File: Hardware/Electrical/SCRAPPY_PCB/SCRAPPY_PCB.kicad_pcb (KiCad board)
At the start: 2 copper layers, 87.6 x 96.5 mm, 54 parts, among them J1 Screw_Terminal_01x02, J2 Conn_01x04, J3 Conn_01x03, J4 Conn_01x03, J5 Conn_01x03, J6 Conn_01x04, J7 Conn_01x04, J8 Conn_01x04, J9 Conn_01x04, Q1 PN2222A, Q2 PN2222A, Q3 PN2222A, U1 ESP32-DevBoard, U2 L7805, U3 LM324

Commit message: Updated PCB; Ready for Manufacture
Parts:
- removed the J7 at (115.6, 133.3)
- added D5: LED, LED_THT:LED_D5.0mm_Clear, F.Cu at (122.5, 91.1)
- added H1: MountingHole, MountingHole:MountingHole_2.2mm_M2_DIN965_Pad, F.Cu at (51.3, 52.3)
- added H2: MountingHole, MountingHole:MountingHole_2.2mm_M2_DIN965_Pad, F.Cu at (135.9, 52.3)
- added H3: MountingHole, MountingHole:MountingHole_2.2mm_M2_DIN965_Pad, F.Cu at (51.3, 143.5)
- added H4: MountingHole, MountingHole:MountingHole_2.2mm_M2_DIN965_Pad, F.Cu at (136.9, 143.5)
- added J11: Conn_02x02_Odd_Even, Connector_PinHeader_2.54mm:PinHeader_1x04_P2.54mm_Vertical, F.Cu at (135.9, 121.9)
- added J3: Conn_02x04_Counter_Clockwise, Connector_PinHeader_2.54mm:PinHeader_2x04_P2.54mm_Vertical, F.Cu at (116.1, 55.7)
- added J6: Conn_01x15, Connector_PinSocket_2.54mm:PinSocket_1x15_P2.54mm_Vertical, F.Cu at (113.0, 96.3)
- added R21: R, Resistor_THT:R_Axial_DIN0207_L6.3mm_D2.5mm_P10.16mm_Horizontal, F.Cu at (128.6, 81.0)
- J9: value Conn_01x04 -> Conn_01x15; footprint Connector_PinHeader_2.54mm:PinHeader_1x04_P2.54mm_Vertical -> Connector_PinSocket_2.54mm:PinSocket_1x15_P2.54mm_Vertical
- Q1, Q2, Q3: footprint Package_TO_SOT_THT:TO-92_Inline -> Package_TO_SOT_THT:TO-92_Inline_Wide
- U2: footprint Converter_DCDC:Converter_DCDC_Murata_OKI-78SR_Horizontal -> Converter_DCDC:Converter_DCDC_RECOM_R-78B-2.0_THT
- moved J7 83.7 mm to (132.0, 103.0), turned to 180 degrees
- moved Q2 70.8 mm to (123.6, 98.3), turned to -90 degrees
- moved J2 68.7 mm to (116.1, 62.1), turned to -90 degrees
- moved R17 60.1 mm to (121.6, 106.9), turned to 0 degrees
- moved R18 54.1 mm to (118.7, 107.4), turned to 90 degrees
- moved R13 44.3 mm to (113.0, 134.9)
- moved J9 37.7 mm to (78.0, 134.3), turned to 180 degrees
- moved DISP1 37.5 mm to (132.3, 129.7), turned to -90 degrees
- moved R14 34.6 mm to (117.1, 126.0), turned to 0 degrees
- moved C9 19.6 mm to (131.1, 78.2), turned to 180 degrees
- moved R10 10.9 mm to (72.6, 89.4), turned to -90 degrees
- moved R11 10.9 mm to (72.6, 102.1), turned to -90 degrees
- moved R20 9.70 mm to (118.5, 121.0), turned to 90 degrees
- moved U2 9.53 mm to (128.6, 69.9)
- moved R19 8.90 mm to (121.5, 120.5)
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- renumbered C4 to C1, C2 to C10, C6 to C2, C7 to C3, C9 to C4, C8 to C5, C10 to C6, C5 to C7, C3 to C8, C1 to C9, D4 to D1, D1 to D2, D2 to D4, J2 to J1, J3 to J10, J8 to J2, J1 to J4, J6 to J5, J4 to J7, J5 to J8, R14 to R1, R23 to R10, R21 to R11, R22 to R12, R11 to R13, R12 to R14, R9 to R15, R10 to R16, R8 to R17, R7 to R18, R6 to R19, R17 to R2, R5 to R20, R16 to R3, R18 to R4, R20 to R5, R13 to R6, R15 to R7, R19 to R8, R24 to R9, RV4 to RV2, RV2 to RV3, RV3 to RV4, U3 to U1, U1 to U3
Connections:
- C9 pad 2: +12V -> +5V
- J2 pad 1: /PIN_1 -> /PIN_3
- J2 pad 3: /PIN_3 -> /PIN_1
- J9 pad 1: GND -> +5V
- J9 pad 2: GND -> +5V
- J9 pad 4: GND -> /RES
- R11 pad 1: +5V -> unconnected-(R11-Pad1)
- R16 pad 1: +3V3 -> +5V
- R17 pad 1: +3V3 -> +5V
- R19 pad 1: +3V3 -> +5V
- U3 pad 11: /PCNT_B -> /SCLK
- U3 pad 12: /PWM_B -> /SDA
- U3 pad 13: /DIR_B -> /RES
- U3 pad 18: /PIN_1 -> /DC
- U3 pad 24: /SCLK -> /PCNT_B
- U3 pad 25: /SDA -> /PWM_B
- U3 pad 26: /HALL-IN_A -> /DIR_B
- U3 pad 27: /HALL-IN_B -> /HALL-IN_A
- U3 pad 28: /PIN_3 -> /HALL-IN_B
- U3 pad 29: /RES -> /PIN_3
- U3 pad 30: /DC -> /PIN_1
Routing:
- net /SCLK: track 0.00 -> 72.7 mm
- net /PIN_2: track 0.00 -> 70.7 mm, vias 0 -> 2
- net /SDA: track 0.00 -> 65.0 mm
- net /RES: track 0.00 -> 58.6 mm, vias 0 -> 1
- net Net-(J2-Pad4): track 0.00 -> 49.3 mm, vias 0 -> 1
- net +3V3: track 0.00 -> 45.0 mm, vias 0 -> 1
- net /PIN_3: track 0.00 -> 42.8 mm, vias 0 -> 1
- net /PIN_1: track 0.00 -> 39.9 mm, vias 0 -> 1
- net /CS: track 0.00 -> 36.0 mm
- net /PCNT_A: track 0.00 -> 32.0 mm, vias 0 -> 1
- net /DIR_A: track 0.00 -> 25.9 mm, vias 0 -> 1
- net /INV_PWM_A: track 0.00 -> 14.6 mm
- net /Aout_B: track 26.3 -> 40.4 mm, vias 0 -> 1
- net /Ain_C: track 71.8 -> 57.9 mm
- net /Aout_A: track 39.9 -> 53.4 mm, vias 0 -> 1
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- added copper zone on F.Cu, net +12V
- removed copper zone on F.Cu, net +3V3
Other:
- board size 87.6 x 96.5 mm -> 91.8 x 98.7 mm
- board text added: "+12V"
- board text added: "2022-SEPT-23"
- board text added: "3V3"
- board text added: "5V"
- board text added: "Ain-A"
- board text added: "Ain-B"
- board text added: "Ain-C"
- board text added: "Ain-D"
- board text added: "By: Matthew Ebert"
- board text added: "C"
- board text added: "CS"
- board text added: "DC"
- board text added: "DIR"
- board text added: "EN"
- board text added: "GND"
- board text added: "HinA"
- board text added: "HinB"
- board text added: "HinC"
- board text added: "HinD"
- board text added: "PCNT"
- board text added: "PIN1"
- board text added: "PIN2"
- board text added: "PIN3"
- board text added: "POWER IND"
- board text added: "PWM"
- board text added: "Project: SCRAPPY Main Controller Board"
- board text added: "R-00"
- board text added: "RES"
- board text added: "SCLK"
- board text added: "SDA"
- board text added: "Vin"
- board text added: "WIFI-KEEP CLEAR"

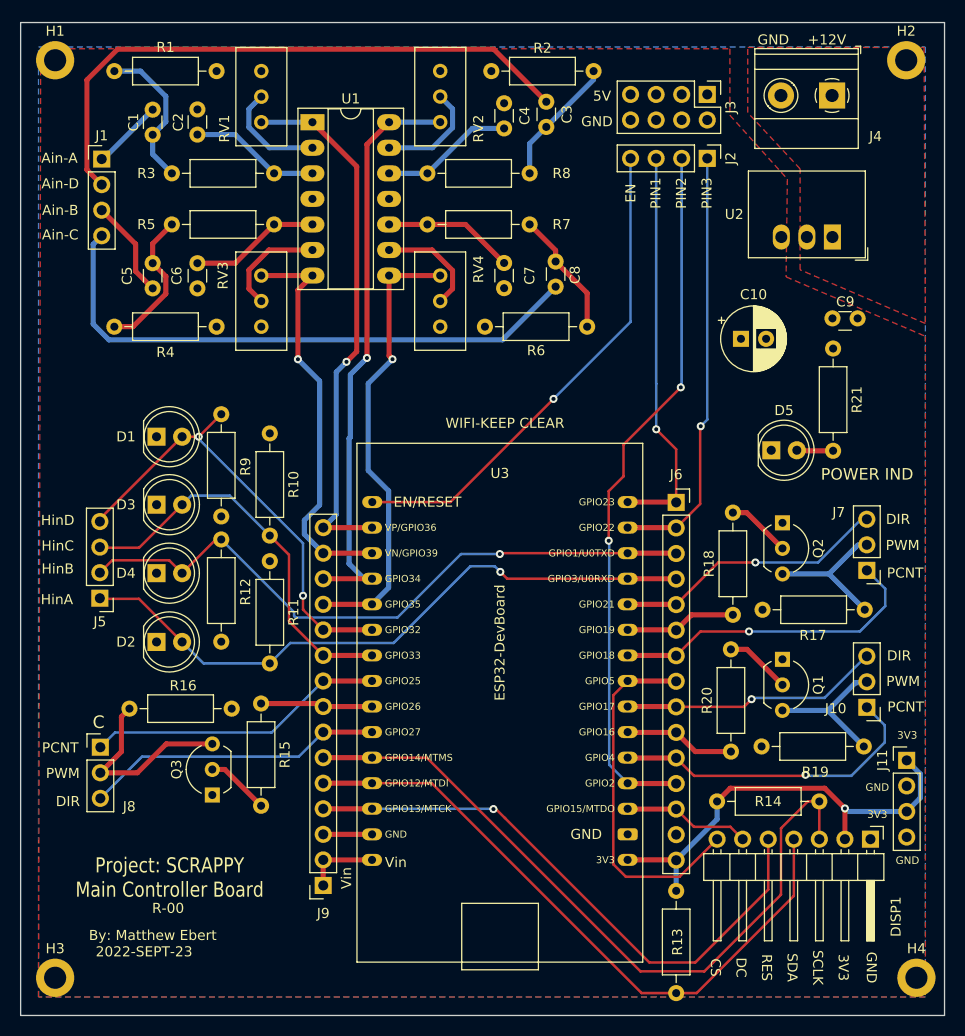
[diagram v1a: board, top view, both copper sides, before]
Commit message: Added Power PCB
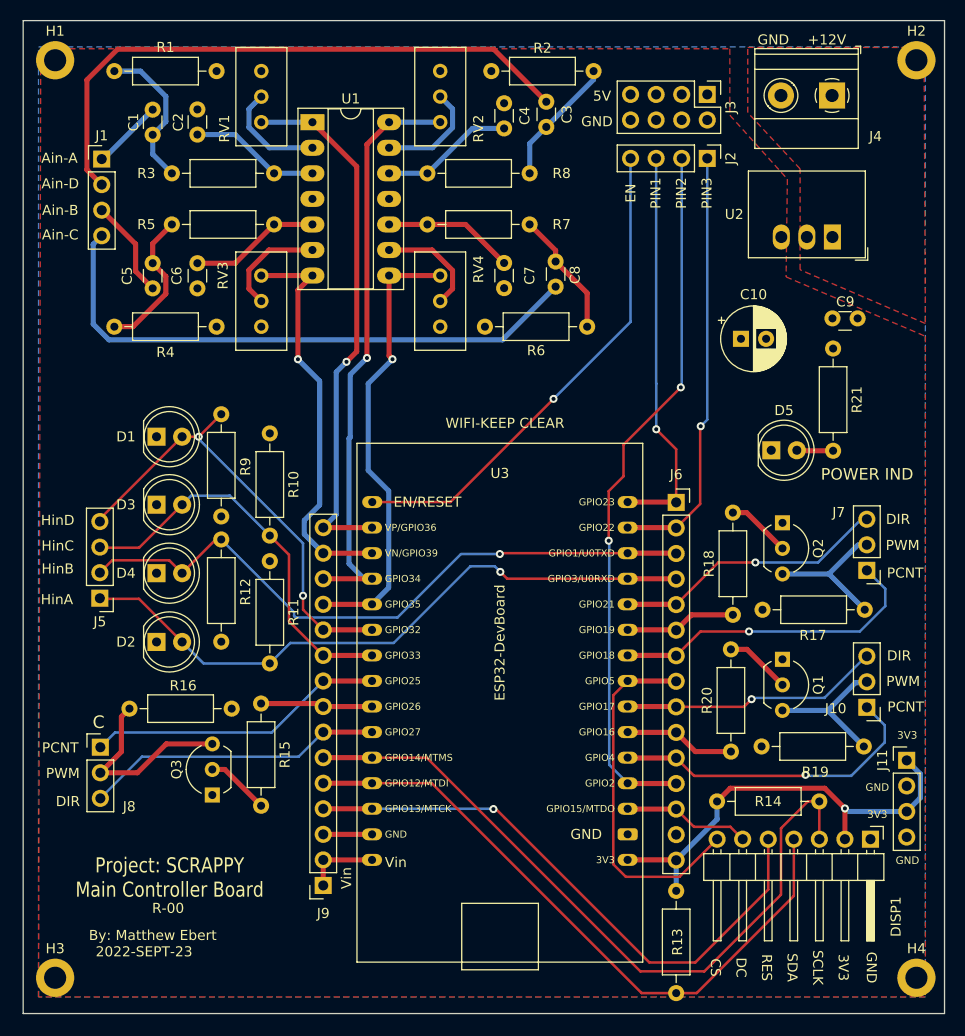
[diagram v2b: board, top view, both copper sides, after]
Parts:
- moved H2 1.02 mm to (136.9, 52.3)
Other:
- board size 91.8 x 98.7 mm -> 91.6 x 98.7 mm
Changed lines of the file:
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@@
   )
   (footprint "MountingHole:MountingHole_2.2mm_M2_DIN965_Pad" (layer "F.Cu")
-    (at 135.89 52.324)
+    (at 136.906 52.324)
     (descr "Mounting Hole 2.2mm, M2, DIN965")
     (tags "mounting hole 2.2mm m2 din965")
@@
     )
   )
-  (gr_rect (start 47.879 48.5775) (end 139.7 147.2565) (layer "Edge.Cuts") (width 0.1) (fill none))
+  (gr_rect (start 48.133 48.387) (end 139.7 147.066) (layer "Edge.Cuts") (width 0.1) (fill none))
   (gr_text "HinC" (at 51.562 100.584) (layer "F.SilkS")
     (effects (font (size 1 1) (thickness 0.15)))
